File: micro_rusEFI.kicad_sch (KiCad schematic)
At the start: 22 parts, among them U3 molex_48pin_MRE

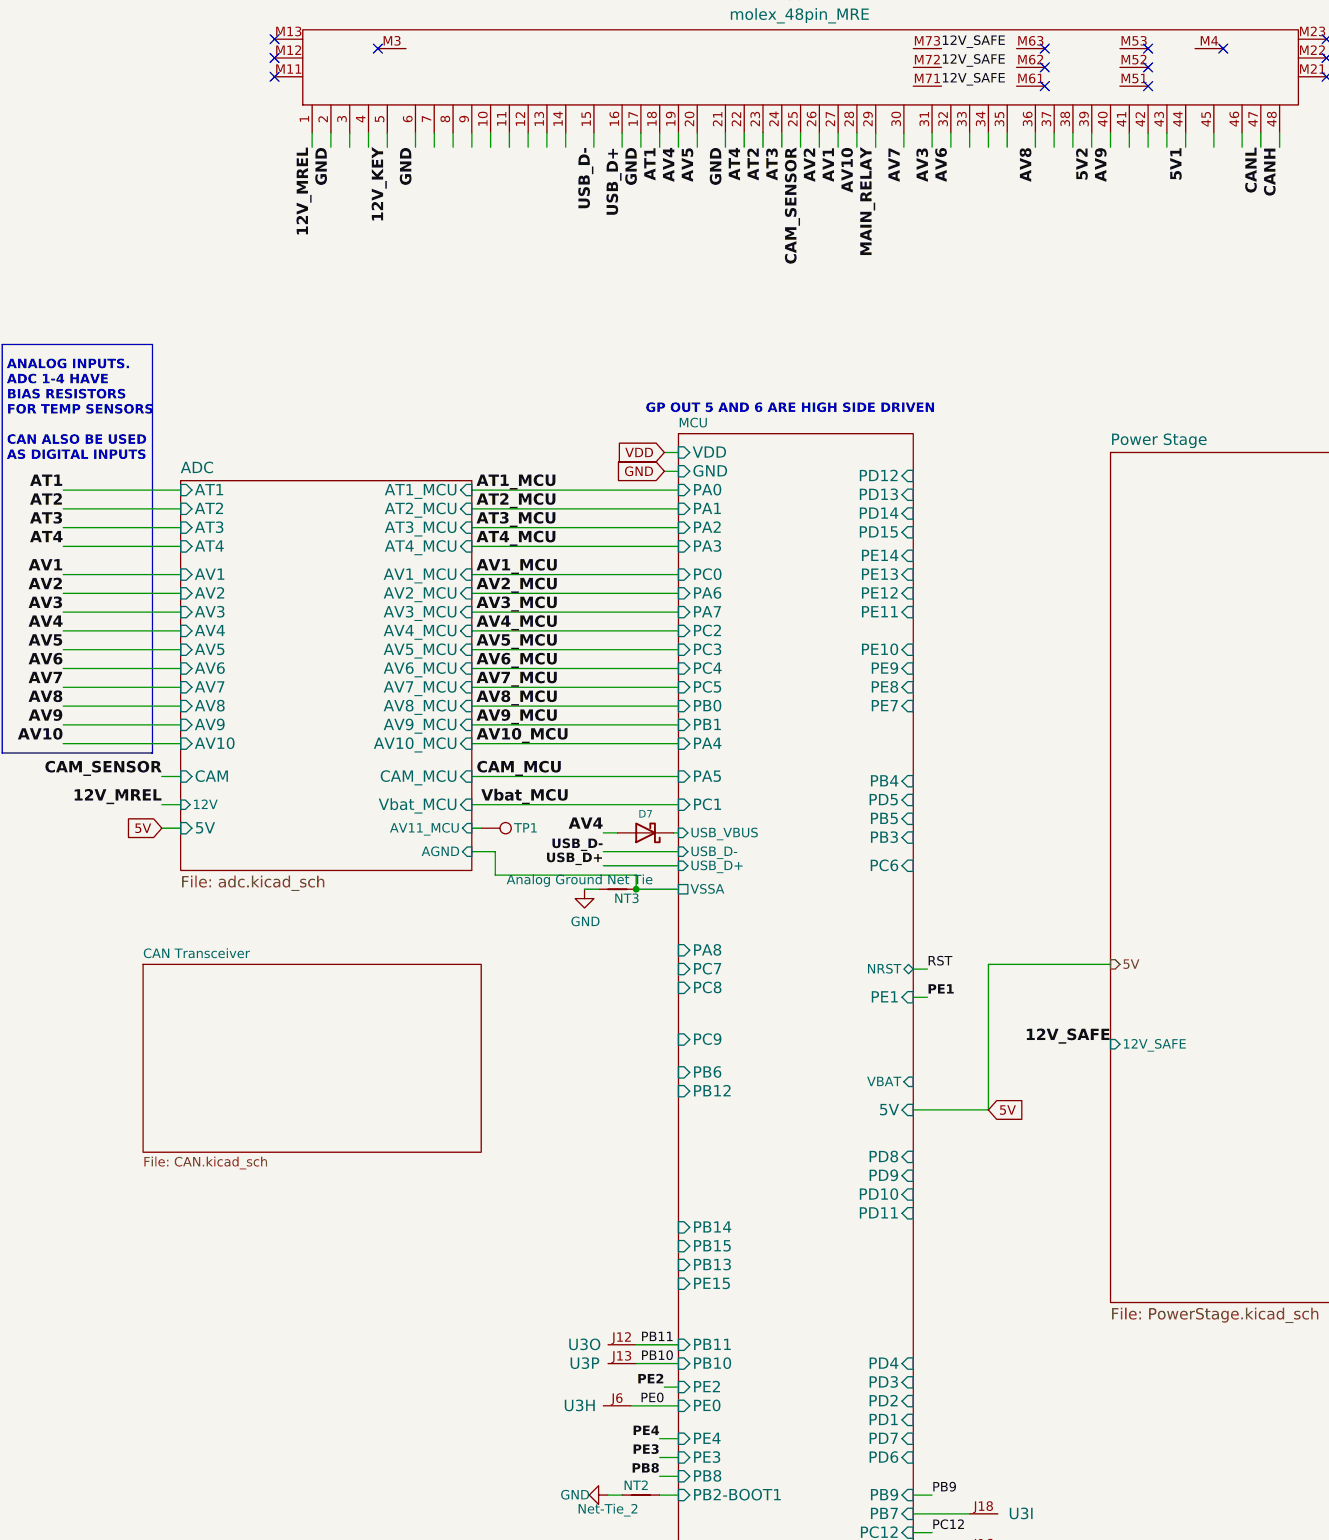
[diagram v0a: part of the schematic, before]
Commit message: 5v supplies added
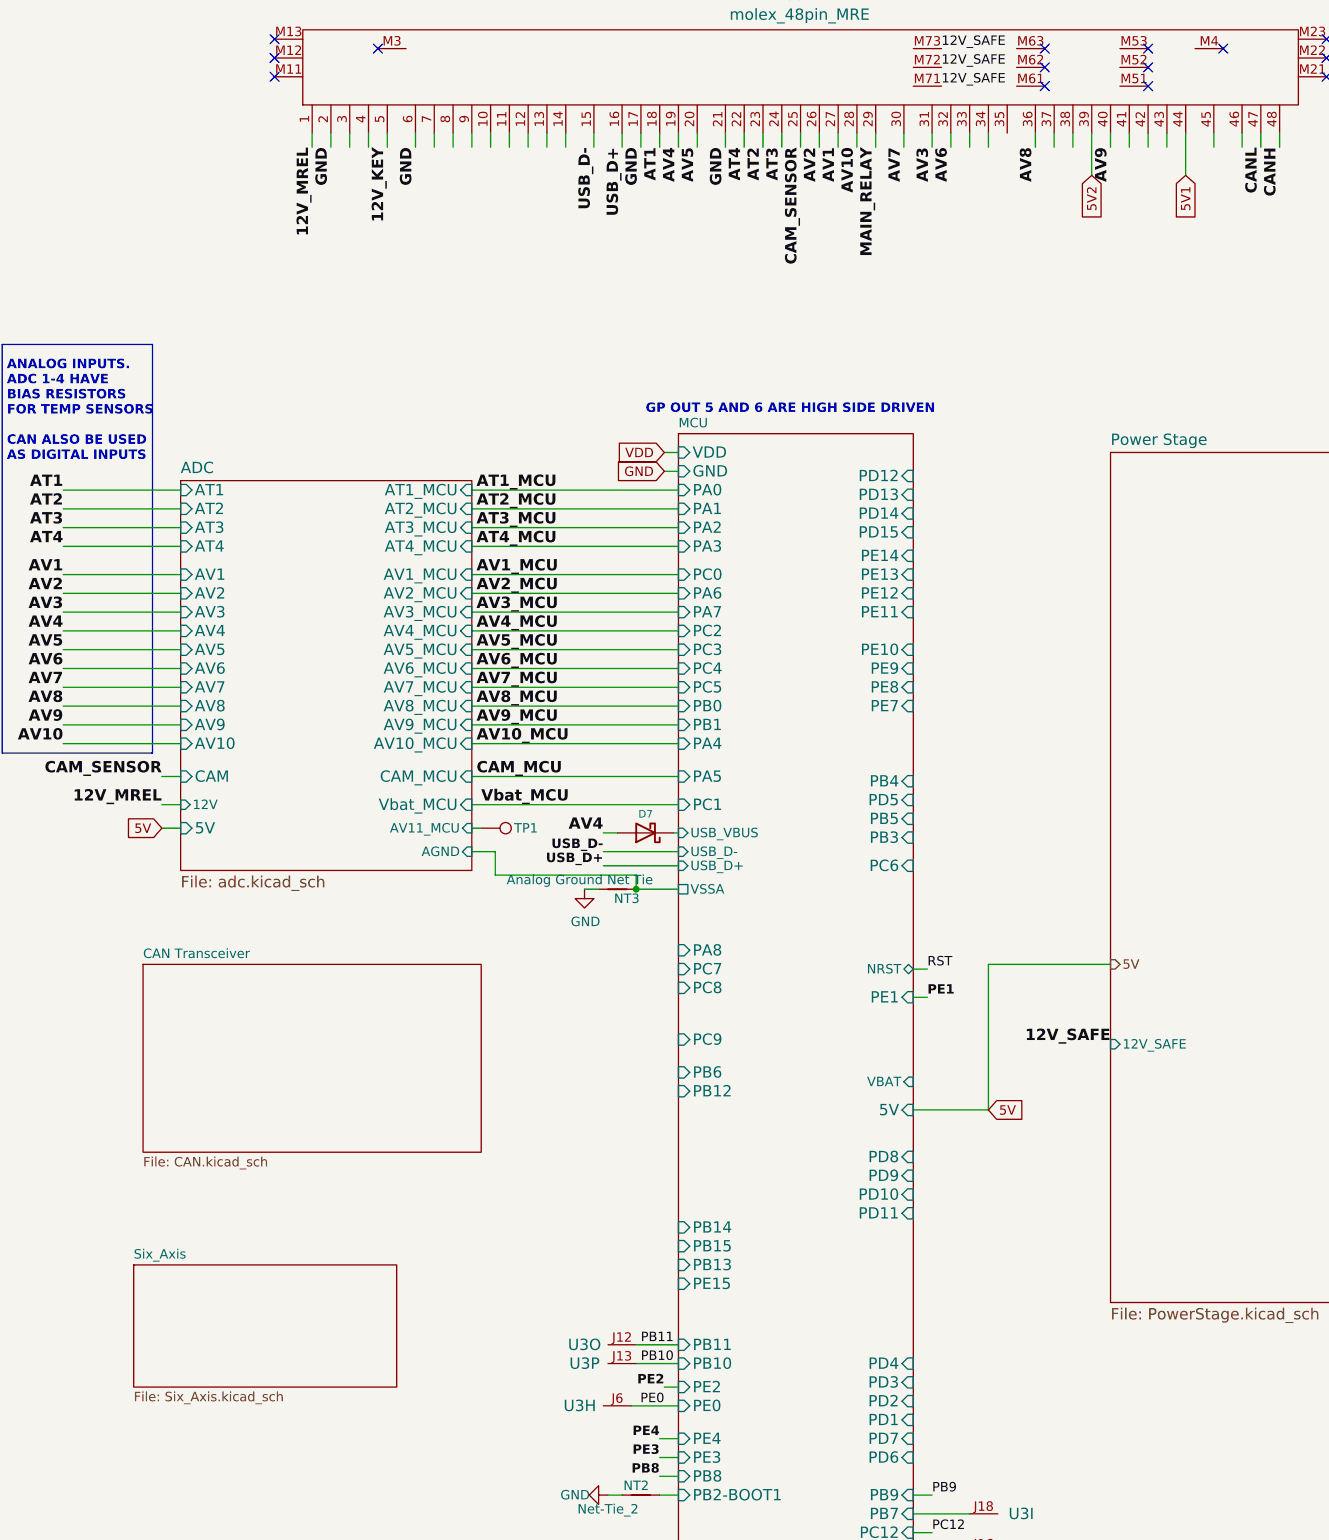
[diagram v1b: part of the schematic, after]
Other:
- added sheet Six_Axis (Six_Axis.kicad_sch)
